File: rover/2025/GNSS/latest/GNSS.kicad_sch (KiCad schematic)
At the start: 31 parts, among them J1 Eth-Horiz, J2 Eth-Horiz, J3 USB_C_USB4105-GF-A, J4 JST6_Pin, SW1 TS09-63-25-WT-160-SMT-TR, SW2 TS09-63-25-WT-160-SMT-TR, U1 SN65HVD232, U2 ESP32-S3-WROVER, U3 LD1086DT33TR, U4 LDO-TLV74033PDBVR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

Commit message: Rev1 pcb gnss
Je vais changer le schematic pour qu'il match le template plus tard.
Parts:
- removed C11: 10uF, Capacitor_SMD:C_0805_2012Metric_Pad1.18x1.45mm_HandSolder, symbol RoverLibrary:C-10uF
- removed C12: 1uF, Capacitor_SMD:C_0805_2012Metric_Pad1.18x1.45mm_HandSolder, symbol RoverLibrary:C_0805
- removed J3: USB_C_USB4105-GF-A, Connector_USB:USB_C_Receptacle_GCT_USB4105-xx-A_16P_TopMnt_Horizontal, symbol RoverLibrary:USB_C_USB4105-GF-A
- removed R3: 10k, Resistor_SMD:R_0805_2012Metric_Pad1.20x1.40mm_HandSolder, symbol RoverLibrary:R-10k
- removed U3: LD1086DT33TR, Package_TO_SOT_SMD:TO-252-2, symbol RoverLibrary:LDO-LD1086DT33TR
- added D1: SB140, Diode_THT:D_DO-41_SOD81_P10.16mm_Horizontal, symbol Diode:SB140
- added J5: USB_C_USB4145-GCT, RoverFootprint:USB4145_GCT, symbol RoverLibrary:USB_C_USB4145-03-C
- added R1: 10k, Resistor_SMD:R_0805_2012Metric_Pad1.20x1.40mm_HandSolder, symbol RoverLibrary:R-10k
- added U3: LDO-LM7805MPX/NOPB, Package_TO_SOT_SMD:SOT-223-3_TabPin2, symbol RoverLibrary:LDO-LM7805MPX/NOPB
- C10: value 10uF -> 22uF
- C5: value 10uF -> 100uF
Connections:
- net 5V_JMPR is gone; now on net +5V: C6.2, JP1.2 (C), U4.1 (INPUT), U4.3 (EN)
- net +24V: now also C10.1, U3.1 (INPUT); no longer C5.2
- net +3.3V: now also C5.1, C9.1, R1.1; no longer C9.2
- net +5V: now also J4.1; no longer JP1.1 (A), U5.1
- net EN_ESP: now also C1.1, C7.2, SW1.1, R1.2; no longer C1.2, C7.1, SW1.2
- net GND: now also C1.2, C10.2, C2.2, C5.2, C7.1, C9.2, SW1.2, J5.A1 (GND), J5.A12 (GND), J5.B1 (GND), J5.B12 (GND), U3.2 (GND); no longer C1.1, C10.1, C2.1, C5.1, C7.2, C9.1, SW1.1
- net GNSS_EN: now also U2.17 (IO9); no longer U2.8 (IO15)
- net GNSS_PPS: now also U2.25 (IO48); no longer U2.21 (IO13)
- net GNSS_RX: now also U2.21 (IO13); no longer U2.17 (IO9)
- net GNSS_TX: now also U2.24 (IO47); no longer U2.19 (IO11)
- net GPIO_0: now also C2.1; no longer C2.2
- net RXC: now also U2.5 (IO5); no longer U2.25 (IO48)
- net TXC: now also U2.4 (IO4); no longer U2.24 (IO47)
- net USB_N: now also J5.A7 (D-), J5.B7 (D-)
- net USB_P: now also J5.A6 (D+), J5.B6 (D+)
- net 5V_U3 renamed +5V_ETH
- net +5V_ETH: now also U3.3 (OUTPUT); no longer C10.2
- new net +5V_USB: D1.1 (K), JP1.1 (A), U5.1
- new net VBUS: D1.2 (A), J5.A4 (VBUS), J5.A9 (VBUS), J5.B4 (VBUS), J5.B9 (VBUS)
- no-connect marks 34 -> 37
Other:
- moved on the sheet: C1, C2, J1, SW1, SW2, U2

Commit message: GNSS Revision (Pas finit)
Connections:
- net EN_ESP: now also C7.1; no longer C7.2
- net GND: now also C7.2; no longer C7.1
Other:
- moved on the sheet: C7, C8, C9, R1, U2

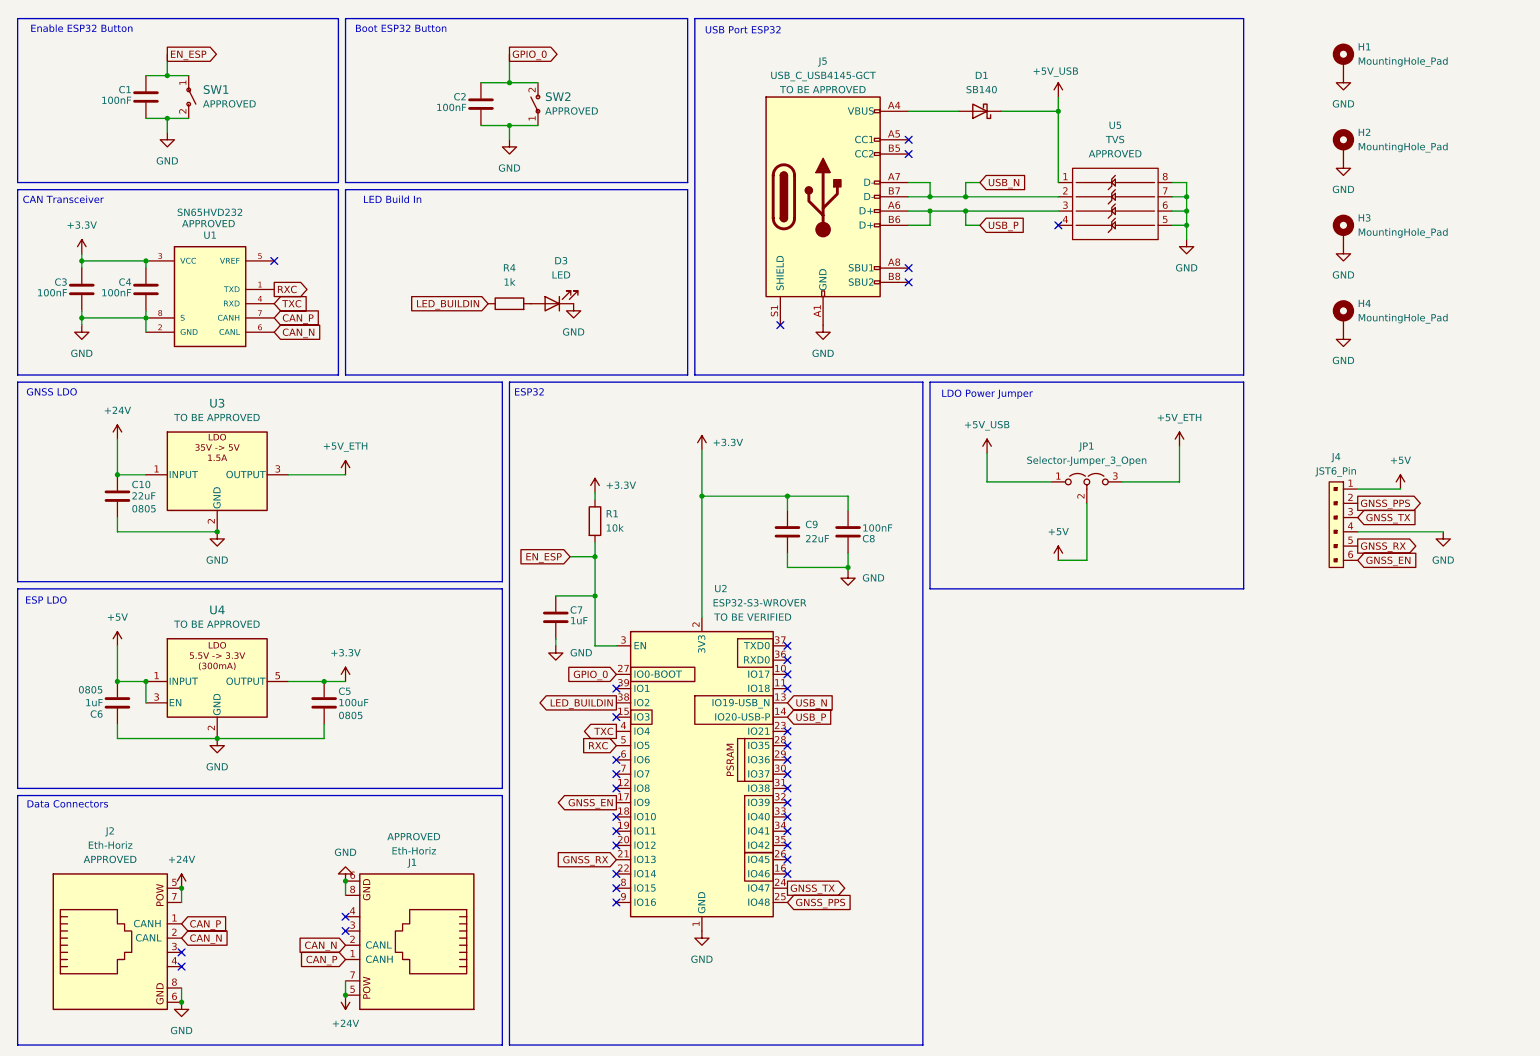
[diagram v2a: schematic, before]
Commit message: ArmJ2 revised for order
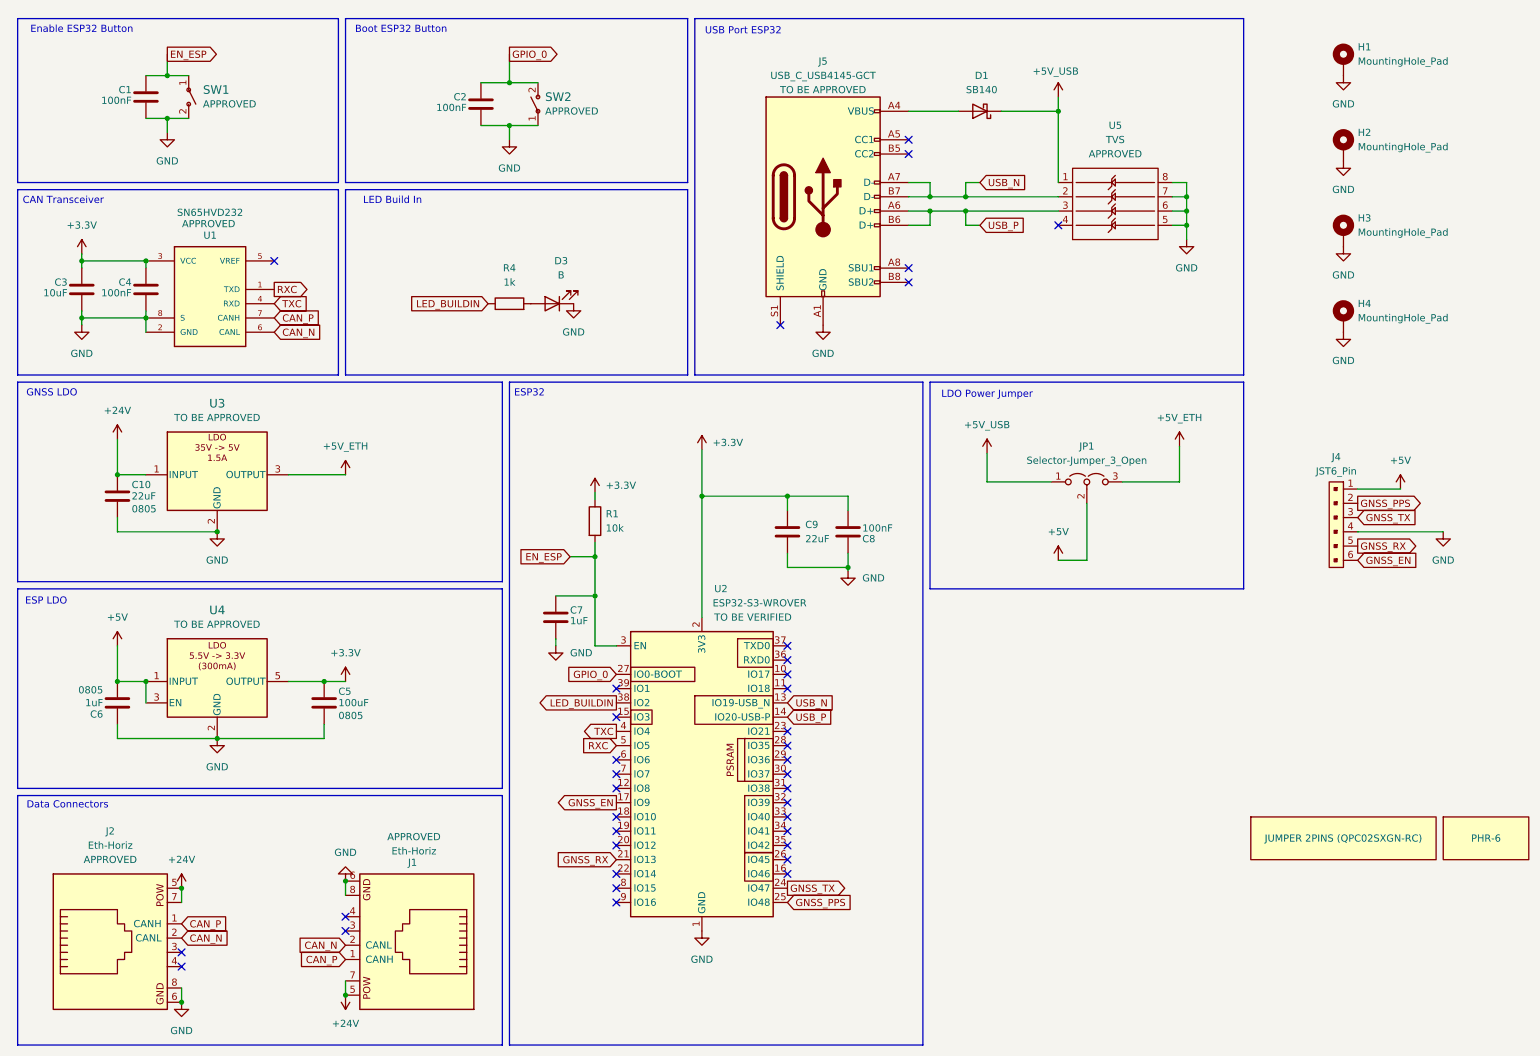
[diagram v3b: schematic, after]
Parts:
- added G1: PHR-6, symbol RoverLibrary:Off Board Part
- added G2: JUMPER 2PINS (QPC02SXGN-RC), symbol RoverLibrary:Off Board Part
- C3: value 100nF -> 10uF
- D3: value LED -> B
- J4: footprint Connector_JST:JST_XH_B6B-XH-AM_1x06_P2.50mm_Vertical -> Connector_JST:JST_PH_B6B-PH-K_1x06_P2.00mm_Vertical
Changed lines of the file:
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@@
 			)
 		)
-		(property "Value" "LED"
+		(property "Value" "B"
 			(at 110.8075 59.69 0)
 			(effects
@@
 	)
 	(symbol
+		(lib_name "Off Board Part_1")
+		(lib_id "RoverLibrary:Off Board Part")
+		(at 250.19 160.02 0)
+		(unit 1)
+		(exclude_from_sim yes)
+		(in_bom yes)
+		(on_board no)
+		(dnp no)
+		(fields_autoplaced yes)
+		(property "Reference" "G2"
+			(at 250.19 118.1801 0)
+			(effects
+				(font
+					(size 1.27 1.27)
+				)
+				(hide yes)
+			)
+		)
+		(property "Value" "JUMPER 2PINS (QPC02SXGN-RC)"
+			(at 250.19 160.02 0)
+			(effects
+				(font
+					(size 1.27 1.27)
+				)
+			)
+		)
+		(property "Footprint" ""
+			(at 247.65 158.75 0)
+			(effects
+				(font
+					(size 1.27 1.27)
+				)
+				(hide yes)
+			)
+		)
+		(property "Datasheet" ""
+			(at 247.65 158.75 0)
+			(effects
+				(font
+					(size 1.27 1.27)
+				)
+				(hide yes)
+			)
+		)
+		(property "Description" ""
+			(at 247.65 158.75 0)
+			(effects
+				(font
+					(size 1.27 1.27)
+				)
+				(hide yes)
+			)
+		)
+		(property "Digikey" "https://www.digikey.ca/en/products/detail/sullins-connector-solutions/QPC02SXGN-RC/2618262"
+			(at 250.19 160.02 0)
+			(effects
+				(font
+					(size 1.27 1.27)
+				)
+				(hide yes)
+			)
+		)
+		(instances
+			(project "GNSS"
+				(path "/42e9f84b-4695-47f8-9ec4-c5ab52c963ba"
+					(reference "G2")
+					(unit 1)
+				)
+			)
+		)
+	)
+	(symbol
 		(lib_id "RoverLibrary:MountingHole_Pad")
 		(at 250.19 36.83 0)
@@
 			)
 		)
-		(property "Footprint" "Connector_JST:JST_XH_B6B-XH-AM_1x06_P2.50mm_Vertical"
+		(property "Footprint" "Connector_JST:JST_PH_B6B-PH-K_1x06_P2.00mm_Vertical"
 			(at 249.555 94.615 0)
 			(effects
@@
 			)
 		)
-		(property "Value" "100nF"
+		(property "Value" "10uF"
 			(at 22.86 62.865 0)
 			(do_not_autoplace yes)
@@
 					(unit 1)
 				)
+			)
+		)
+	)
+	(symbol
+		(lib_name "Off Board Part_2")
+		(lib_id "RoverLibrary:Off Board Part")
+		(at 275.59 160.02 0)
+		(unit 1)
+		(exclude_from_sim yes)
+		(in_bom yes)
+		(on_board no)
+		(dnp no)
+		(fields_autoplaced yes)
+		(property "Reference" "G1"
+			(at 275.59 118.1801 0)
+			(effects
+				(font
+					(size 1.27 1.27)
+				)
+				(hide yes)
+			)
+		)
+		(property "Value" "PHR-6"
+			(at 275.59 160.02 0)
+			(do_not_autoplace yes)
+			(effects
+				(font
+					(size 1.27 1.27)
+				)
+			)
+		)
+		(property "Footprint" ""
+			(at 273.05 158.75 0)
+			(effects
+				(font
+					(size 1.27 1.27)
+				)
+				(hide yes)
+			)
+		)
+		(property "Datasheet" ""
+			(at 273.05 158.75 0)
+			(effects
+				(font
+					(size 1.27 1.27)
+				)
+				(hide yes)
+			)
+		)
+		(property "Description" ""
+			(at 273.05 158.75 0)
+			(effects
+				(font
+					(size 1.27 1.27)
+				)
+				(hide yes)
+			)
+		)
+		(property "Digikey" "https://www.digikey.ca/en/products/detail/jst-sales-america-inc/PHR-6/608604"
+			(at 275.59 162.814 0)
+			(effects
+				(font
+					(size 1.27 1.27)
+				)
+				(hide yes)
+			)
+		)
+		(instances
+			(project "GNSS"
+				(path "/42e9f84b-4695-47f8-9ec4-c5ab52c963ba"
+					(reference "G1")
+					(unit 1)
+				)

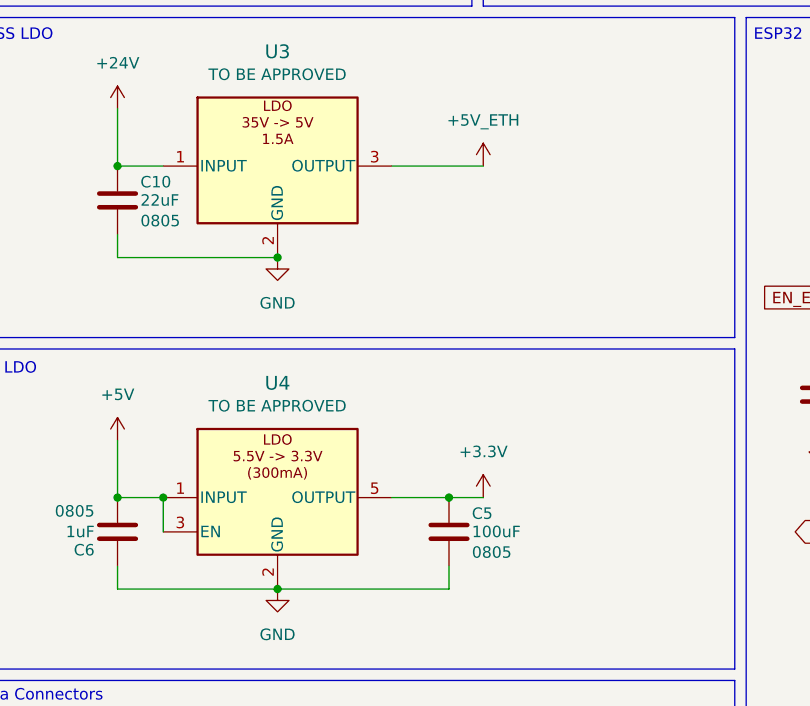
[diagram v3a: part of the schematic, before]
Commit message: GNSS Petits changements
Jacob était à côté de moi quand j'ai ouvert le pcb et il m'a aidé.

- Skew dans les traces différentielles USB et CAN réglé.
- Pour le USB, une des deux traces différentielles doit passer à travers des vias afin de swap les deux signaux de côté. Donc, la trace qui ne passe pas par des vias est une épaisseur de board plus longue.

- Texte pour le connecteur de GNSS flippé pour qu'il soit du bon sens

- Traces 24V de CAN élargies de 12 mil à 15 mil

-  Ajout d'un condensateur de sortie de 100nF au LDO 35-5 (U3)

- Changement de la valeur du condensateur de sortie du LDO 5.5-3.3 de 100uF à 10uF

- Un des connecteurs eth bougé un peu pour laisser plus de clearance au mounting hole
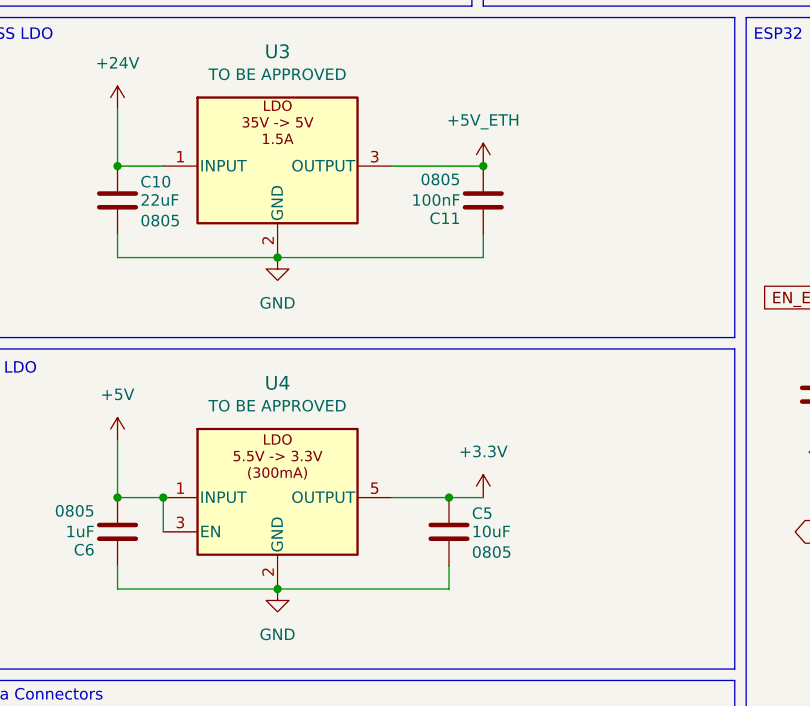
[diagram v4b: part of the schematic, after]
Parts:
- added C11: 100nF, Capacitor_SMD:C_0805_2012Metric_Pad1.18x1.45mm_HandSolder, symbol Rover_Library:C_0805
- C5: value 100uF -> 10uF
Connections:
- net +5V_ETH: now also C11.2
- net GND: now also C11.1
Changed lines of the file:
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@@
 	(paper "A4")
 	(junction
+		(at 72.39 95.25)
+		(diameter 0)
+		(color 0 0 0 0)
+	)
+	(junction
 		(at 36.83 57.15)
 		(diameter 0)
@@
 	(wire
 		(pts
+			(xy 49.53 105.41) (xy 72.39 105.41)
+		)
+		(stroke
+			(width 0)
+			(type default)
+		)
+	)
+	(wire
+		(pts
 			(xy 101.6 33.02) (xy 106.68 33.02)
 		)
@@
 	(wire
 		(pts
+			(xy 72.39 105.41) (xy 72.39 102.87)
+		)
+		(stroke
+			(width 0)
+			(type default)
+		)
+	)
+	(wire
+		(pts
 			(xy 36.83 67.31) (xy 36.83 69.85)
 		)
@@
 	)
 	(symbol
+		(lib_id "Rover_Library:C_0805")
+		(at 72.39 99.06 180)
+		(unit 1)
+		(exclude_from_sim no)
+		(in_bom yes)
+		(on_board yes)
+		(dnp no)
+		(fields_autoplaced yes)
+		(property "Reference" "C11"
+			(at 69.85 101.092 0)
+			(do_not_autoplace yes)
+			(effects
+				(font
+					(size 1.27 1.27)
+				)
+				(justify left)
+			)
+		)
+		(property "Value" "100nF"
+			(at 69.85 99.06 0)
+			(do_not_autoplace yes)
+			(effects
+				(font
+					(size 1.27 1.27)
+				)
+				(justify left)
+			)
+		)
+		(property "Footprint" "Capacitor_SMD:C_0805_2012Metric_Pad1.18x1.45mm_HandSolder"
+			(at 70.7898 88.265 0)
+			(effects
+				(font
+					(size 1.27 1.27)
+				)
+				(hide yes)
+			)
+		)
+		(property "Datasheet" "~"
+			(at 71.755 88.265 0)
+			(effects
+				(font
+					(size 1.27 1.27)
+				)
+				(hide yes)
+			)
+		)
+		(property "Description" "Unpolarized capacitor"
+			(at 71.755 88.265 0)
+			(effects
+				(font
+					(size 1.27 1.27)
+				)
+				(hide yes)
+			)
+		)
+		(property "Package" "0805"
+			(at 69.85 96.774 0)
+			(do_not_autoplace yes)
+			(effects
+				(font
+					(size 1.27 1.27)
+				)
+				(justify left)
+			)
+		)
+		(pin "2"
+		)
+		(pin "1"
+		)
+		(instances
+			(project ""
+				(path "/42e9f84b-4695-47f8-9ec4-c5ab52c963ba"
+					(reference "C11")
+					(unit 1)
+				)
+			)
+		)
+	)
+	(symbol
 		(lib_id "RoverLibrary:MountingHole_Pad")
 		(at 250.19 67.31 0)
@@
 			)
 		)
-		(property "Value" "100uF"
+		(property "Value" "10uF"
 			(at 71.12 135.89 0)
 			(do_not_autoplace yes)

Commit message: Gnss condo modifs
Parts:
- added C12: 10uF, Capacitor_SMD:C_0805_2012Metric_Pad1.18x1.45mm_HandSolder, symbol RoverLibrary:C_0805
- C10, C9: value 22uF -> 10uF
- C3: value 10uF -> 22uF
- C6: value 1uF -> 10uF
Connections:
- net +5V: now also C6.1; no longer C6.2
- net +5V_ETH: now also C11.1, C12.1; no longer C11.2
- net GND: now also C11.2, C6.2, C12.2; no longer C11.1, C6.1
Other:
- moved on the sheet: C10, C11, C6, U3

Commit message: HighAmp generated
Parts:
- C3: value 22uF -> 10uF
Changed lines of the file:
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@@
 	(paper "A4")
 	(junction
+		(at 82.55 96.52)
+		(diameter 0)
+		(color 0 0 0 0)
+	)
+	(junction
 		(at 71.12 96.52)
 		(diameter 0)
@@
 	(wire
 		(pts
+			(xy 82.55 96.52) (xy 71.12 96.52)
+		)
+		(stroke
+			(width 0)
+			(type default)
+		)
+	)
+	(wire
+		(pts
 			(xy 116.84 109.855) (xy 116.84 116.84)
 		)
@@
 	(wire
 		(pts
-			(xy 71.12 96.52) (xy 82.55 96.52)
-		)
-		(stroke
-			(width 0)
-			(type default)
-		)
-	)
-	(wire
-		(pts
 			(xy 82.55 104.14) (xy 82.55 106.68)
 		)
@@
 	(symbol
 		(lib_id "power:+5V")
-		(at 71.12 96.52 0)
+		(at 82.55 96.52 0)
 		(unit 1)
 		(exclude_from_sim no)
@@
 		(fields_autoplaced yes)
 		(property "Reference" "#PWR035"
-			(at 71.12 100.33 0)
+			(at 82.55 100.33 0)
 			(effects
 				(font
@@
 		)
 		(property "Value" "+5V_ETH"
-			(at 71.12 91.44 0)
+			(at 82.55 91.44 0)
 			(effects
 				(font
@@
 		)
 		(property "Footprint" ""
-			(at 71.12 96.52 0)
+			(at 82.55 96.52 0)
 			(effects
 				(font
@@
 		)
 		(property "Datasheet" ""
-			(at 71.12 96.52 0)
+			(at 82.55 96.52 0)
 			(effects
 				(font
@@
 		)
 		(property "Description" "Power symbol creates a global label with name \"+5V\""
-			(at 71.12 96.52 0)
+			(at 82.55 96.52 0)
 			(effects
 				(font
@@
 			)
 		)
-		(property "Value" "22uF"
+		(property "Value" "10uF"
 			(at 22.86 62.865 0)
 			(do_not_autoplace yes)
